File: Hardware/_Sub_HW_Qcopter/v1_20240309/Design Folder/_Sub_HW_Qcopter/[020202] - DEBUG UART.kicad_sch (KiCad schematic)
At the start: 3 parts, among them J2801 HDR_1X3_THD-1.27MM

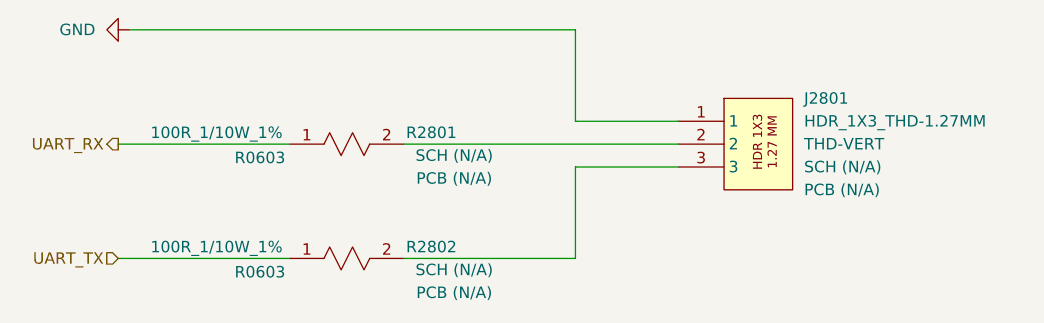
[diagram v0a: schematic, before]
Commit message: Update [020202] - DEBUG UART.kicad_sch
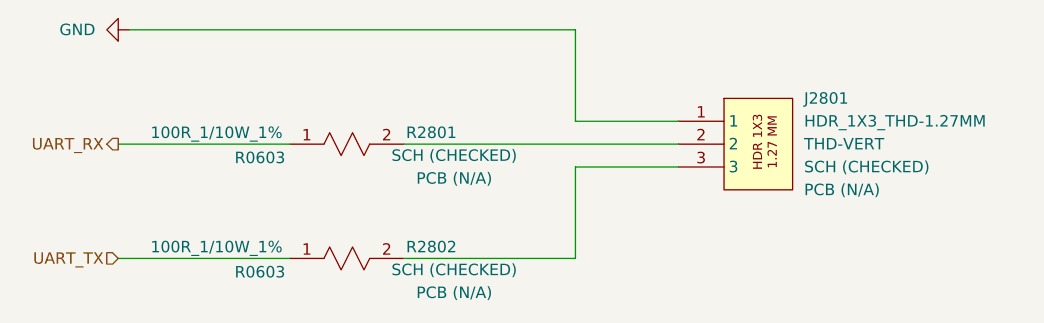
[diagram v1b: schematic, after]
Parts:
- J2801, R2801, R2802: SCH CHECK SCH (N/A) -> SCH (CHECKED)
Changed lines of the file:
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@@
 			)
 		)
-		(property "SCH CHECK" "SCH (N/A)"
+		(property "SCH CHECK" "SCH (CHECKED)"
 			(at 279.4 167.6399 0)
 			(effects
@@
 			)
 		)
-		(property "SCH CHECK" "SCH (N/A)"
+		(property "SCH CHECK" "SCH (CHECKED)"
 			(at 240.538 166.37 0)
 			(effects
@@
 			)
 		)
-		(property "SCH CHECK" "SCH (N/A)"
+		(property "SCH CHECK" "SCH (CHECKED)"
 			(at 240.538 179.07 0)
 			(effects
